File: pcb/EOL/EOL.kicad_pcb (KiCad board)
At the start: 2 copper layers, 51 x 44.5 mm, 28 parts, among them J1 Screw_Terminal_01x02, J2 Screw_Terminal_01x02, J3 Screw_Terminal_01x02, SW1 Slide_DPDT, SW2 Slide_DPDT, SW3 Slide_DPDT, SW4 Slide_DPDT, SW5 SW_Push_DPDT, SW6 SW_Push_DPDT, SW7 SW_Push_DPDT

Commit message: Changed from screw terminal to push terminals
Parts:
- removed J2, J3: Screw_Terminal_01x02, TerminalBlock:TerminalBlock_bornier-2_P5.08mm
- J1: value Screw_Terminal_01x02 -> Conn_01x06; footprint TerminalBlock:TerminalBlock_bornier-2_P5.08mm -> External:PHOENIX_1985234
- moved J1 4.09 mm to (31.9, 14.5), turned to 0 degrees
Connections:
- J1 pad 1: IN1 -> SLS1
- J1 pad 2: Net-(J1-Pad2) -> IN1
- R1 pad 2: Net-(J2-Pad2) -> SLC1
- SW1 pad 1: Net-(SW1-Pad1) -> unconnected-(SW1-Pad1)
- SW1 pad 2: Net-(SW1-Pad2) -> unconnected-(SW1-Pad2)
- SW1 pad 3: Net-(SW1-Pad3) -> unconnected-(SW1-Pad3)
- SW1 pad 4: Net-(SW1-Pad4) -> unconnected-(SW1-Pad4)
- SW2 pad 2: Net-(J3-Pad2) -> DL
- SW2 pad 4: Net-(SW2-Pad4) -> unconnected-(SW2-Pad4)
- SW2 pad 5: Net-(SW2-Pad5) -> unconnected-(SW2-Pad5)
- SW2 pad 6: Net-(SW2-Pad6) -> unconnected-(SW2-Pad6)
- SW3 pad 2: Net-(J1-Pad2) -> SLS1
- SW3 pad 4: Net-(SW3-Pad4) -> unconnected-(SW3-Pad4)
- SW3 pad 5: Net-(SW3-Pad5) -> unconnected-(SW3-Pad5)
- SW3 pad 6: Net-(SW3-Pad6) -> unconnected-(SW3-Pad6)
- SW4 pad 1: Net-(SW4-Pad1) -> unconnected-(SW4-Pad1)
- SW4 pad 2: Net-(SW4-Pad2) -> unconnected-(SW4-Pad2)
- SW4 pad 3: Net-(SW4-Pad3) -> unconnected-(SW4-Pad3)
- SW4 pad 4: Net-(SW4-Pad4) -> unconnected-(SW4-Pad4)
- SW5 pad 1: Net-(SW5-Pad1) -> unconnected-(SW5-Pad1)
- SW5 pad 2: Net-(J2-Pad2) -> SLC1
- SW5 pad 4: Net-(SW5-Pad4) -> unconnected-(SW5-Pad4)
- SW5 pad 5: Net-(SW5-Pad5) -> unconnected-(SW5-Pad5)
- SW5 pad 6: Net-(SW5-Pad6) -> unconnected-(SW5-Pad6)
- SW6 pad 1: Net-(SW6-Pad1) -> unconnected-(SW6-Pad1)
- SW6 pad 4: Net-(SW6-Pad4) -> unconnected-(SW6-Pad4)
- SW6 pad 5: Net-(SW6-Pad5) -> unconnected-(SW6-Pad5)
- SW6 pad 6: Net-(SW6-Pad6) -> unconnected-(SW6-Pad6)
- SW7 pad 1: Net-(SW7-Pad1) -> unconnected-(SW7-Pad1)
- SW7 pad 4: Net-(SW7-Pad4) -> unconnected-(SW7-Pad4)
- SW7 pad 5: Net-(SW7-Pad5) -> unconnected-(SW7-Pad5)
- SW7 pad 6: Net-(SW7-Pad6) -> unconnected-(SW7-Pad6)
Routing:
- net SLC1: track 0.00 -> 25.6 mm
- net Net-(J2-Pad2): track 25.6 -> 0.00 mm
- net SLS1: track 0.00 -> 14.5 mm
- net Net-(J3-Pad2): track 14.5 -> 0.00 mm
- net Net-(J1-Pad2): track 14.5 -> 0.00 mm
- net DL: track 0.00 -> 14.5 mm
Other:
- board size 51 x 44.5 mm -> 51 x 47.5 mm
- net class Default removed
- board text removed: "GND"
- board text removed: "V+"

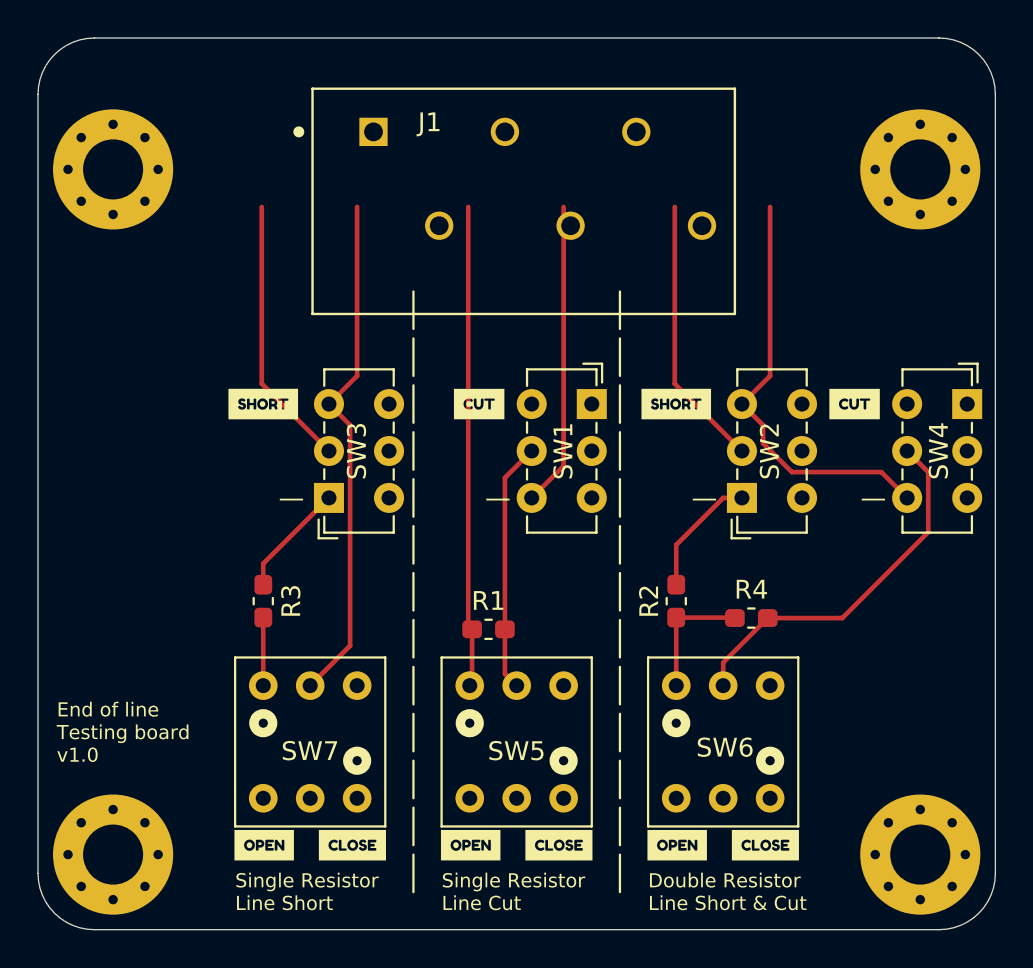
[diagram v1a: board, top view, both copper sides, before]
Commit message: New 3d model, transition to kicad v6
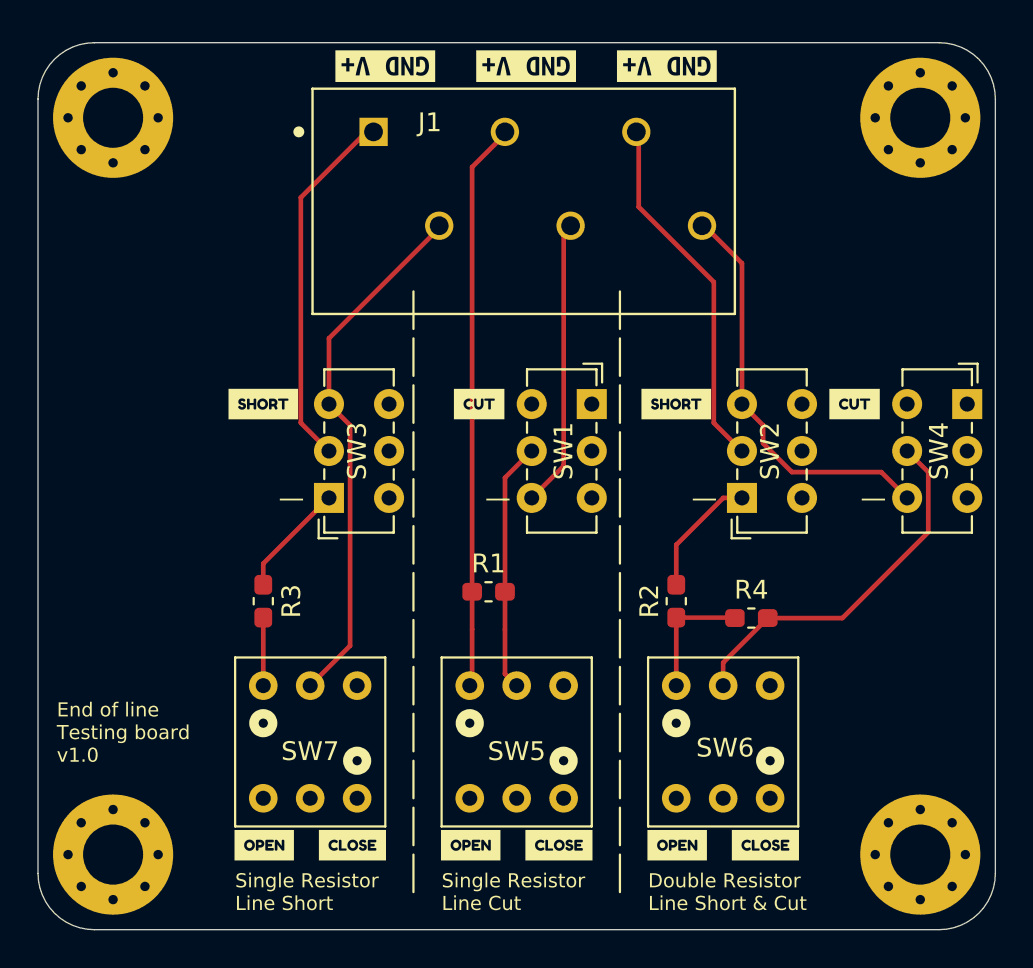
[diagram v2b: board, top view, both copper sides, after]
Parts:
- added kibuzzard-624DDF7A: G***, kibuzzard-624DDF7A, F.Cu at (40.0, 11.0)
- added kibuzzard-624DDF7A: G***, kibuzzard-624DDF7A, F.Cu at (47.5, 11.0)
- added kibuzzard-624DDF7A: G***, kibuzzard-624DDF7A, F.Cu at (32.5, 11.0)
- moved H2 2.75 mm to (61.0, 13.8)
- moved H3 2.75 mm to (18.0, 13.8)
- moved R1 2.00 mm to (38.0, 39.0)
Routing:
- net DL: track 14.5 -> 19.3 mm
- net SLS1: track 14.5 -> 19.1 mm
- net SLC1: track 25.6 -> 30.2 mm
- net IN1: track 27.5 -> 28.3 mm
- net IN3: track 22.6 -> 21.8 mm
- net IN2: track 16.2 -> 15.4 mm
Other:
- board size 51 x 47.5 mm -> 51 x 47.2 mm

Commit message: Minor changes.
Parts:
- moved kibuzzard-624DDF7A 1.30 mm to (46.2, 11.0)
- moved kibuzzard-624DDF7A 0.80 mm to (39.2, 11.0)
- moved kibuzzard-624DDF7A 0.50 mm to (32.0, 11.0)
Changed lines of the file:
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@@
   )
   (footprint "kibuzzard-624DDF7A" (layer "F.Cu")
-    (at 40 11 180)
+    (at 39.2 11 180)
     (descr "Generated with KiBuzzard")
     (tags "kb_params=eyJBbGlnbm1lbnRDaG9pY2UiOiAiQ2VudGVyIiwgIkNhcExlZnRDaG9pY2UiOiAiWyIsICJDYXBSaWdodENob2ljZSI6ICJdIiwgIkZvbnRDb21ib0JveCI6ICJVYnVudHVNb25vLUIiLCAiSGVpZ2h0Q3RybCI6ICIxIiwgIkxheWVyQ29tYm9Cb3giOiAiRi5TaWxrUyIsICJNdWx0aUxpbmVUZXh0IjogIkdORCBWKyIsICJQYWRkaW5nQm90dG9tQ3RybCI6ICI1IiwgIlBhZGRpbmdMZWZ0Q3RybCI6ICI1IiwgIlBhZGRpbmdSaWdodEN0cmwiOiAiNSIsICJQYWRkaW5nVG9wQ3RybCI6ICI1IiwgIldpZHRoQ3RybCI6ICIifQ==")
@@
   )
   (footprint "kibuzzard-624DDF7A" (layer "F.Cu")
-    (at 47.5 11 180)
+    (at 46.2 11 180)
     (descr "Generated with KiBuzzard")
     (tags "kb_params=eyJBbGlnbm1lbnRDaG9pY2UiOiAiQ2VudGVyIiwgIkNhcExlZnRDaG9pY2UiOiAiWyIsICJDYXBSaWdodENob2ljZSI6ICJdIiwgIkZvbnRDb21ib0JveCI6ICJVYnVudHVNb25vLUIiLCAiSGVpZ2h0Q3RybCI6ICIxIiwgIkxheWVyQ29tYm9Cb3giOiAiRi5TaWxrUyIsICJNdWx0aUxpbmVUZXh0IjogIkdORCBWKyIsICJQYWRkaW5nQm90dG9tQ3RybCI6ICI1IiwgIlBhZGRpbmdMZWZ0Q3RybCI6ICI1IiwgIlBhZGRpbmdSaWdodEN0cmwiOiAiNSIsICJQYWRkaW5nVG9wQ3RybCI6ICI1IiwgIldpZHRoQ3RybCI6ICIifQ==")
@@
   )
   (footprint "kibuzzard-624DDF7A" (layer "F.Cu")
-    (at 32.5 11 180)
+    (at 32 11 180)
     (descr "Generated with KiBuzzard")
     (tags "kb_params=eyJBbGlnbm1lbnRDaG9pY2UiOiAiQ2VudGVyIiwgIkNhcExlZnRDaG9pY2UiOiAiWyIsICJDYXBSaWdodENob2ljZSI6ICJdIiwgIkZvbnRDb21ib0JveCI6ICJVYnVudHVNb25vLUIiLCAiSGVpZ2h0Q3RybCI6ICIxIiwgIkxheWVyQ29tYm9Cb3giOiAiRi5TaWxrUyIsICJNdWx0aUxpbmVUZXh0IjogIkdORCBWKyIsICJQYWRkaW5nQm90dG9tQ3RybCI6ICI1IiwgIlBhZGRpbmdMZWZ0Q3RybCI6ICI1IiwgIlBhZGRpbmdSaWdodEN0cmwiOiAiNSIsICJQYWRkaW5nVG9wQ3RybCI6ICI1IiwgIldpZHRoQ3RybCI6ICIifQ==")

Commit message: New design
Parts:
- added kibuzzard-6255E20F: G***, kibuzzard-6255E20F, F.Cu at (18.2, 42.8)
- added kibuzzard-6255E264: G***, kibuzzard-6255E264, F.Cu at (18.2, 35.8)
- added kibuzzard-6255E2F9: G***, kibuzzard-6255E2F9, F.Cu at (24.6, 39.4)
- added kibuzzard-6255E2F9: G***, kibuzzard-6255E2F9, F.Cu at (52.0, 41.8)
- added kibuzzard-6255E2F9: G***, kibuzzard-6255E2F9, F.Cu at (38.0, 40.4)
- added kibuzzard-6255E32D: G***, kibuzzard-6255E32D, F.Cu at (49.4, 39.6)
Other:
- board text removed: "End of line Testing board v1.0"
